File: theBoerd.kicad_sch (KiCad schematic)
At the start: 181 parts, among them SW1 SW_Push, U2 TRRS, U3 BlackPill_STLINK

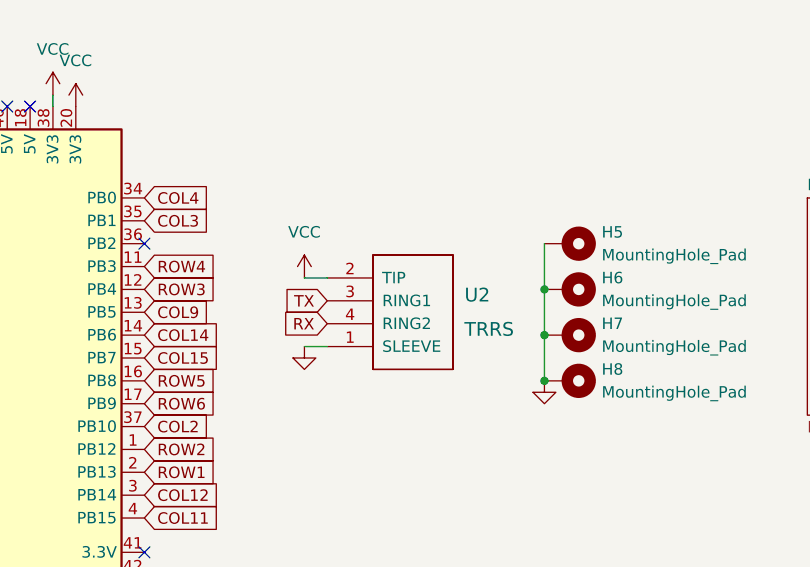
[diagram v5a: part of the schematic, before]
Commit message: Diode and Jack fixes, Silkscreen additons
Diode and TRRS Jack footprints replaced with available parts.
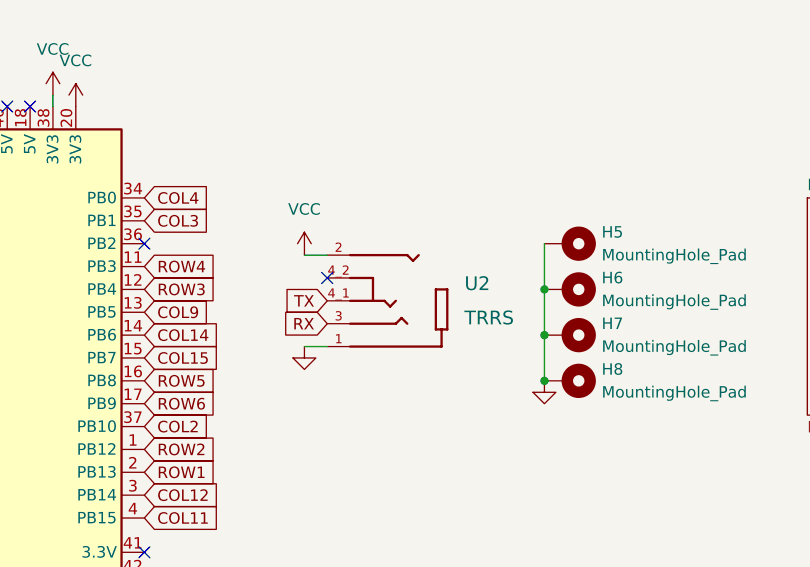
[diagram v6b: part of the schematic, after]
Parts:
- D1, D10, D11, D12, D13, D14, D15, D16, D17, D18, D19, D2, D20, D21, D22, D23, D24, D25, D26, D27, D28, D29, D3, D30, D31, D32, D33, D34, D35, D36, D37, D38, D39, D4, D40, D41, D42, D43, D44, D45, D46, D47, D48, D49, D5, D50, D51, D52, D53, D54, D55, D56, D57, D58, D59, D6, D60, D61, D62, D63, D64, D65, D66, D67, D68, D69, D7, D70, D71, D72, D73, D74, D75, D76, D77, D78, D79, D8, D80, D81, D82, D83, D84, D85, D86, D87, D9: footprint Diode_SMD:D_1210_3225Metric -> Diode_SMD:D_SOD-323_HandSoldering
- U2: footprint Keebio-Parts:TRRS-PJ-320A -> 54_00174:TENSILITY_54-00174; symbol keebio:TRRS -> 54-00174:54-00174; MANUFACTURER (none) -> TENSILITY; MAXIMUM_PACKAGE_HEIGHT (none) -> 6mm; PARTREV (none) -> A; SNAPEDA_PN (none) -> 54-00174; STANDARD (none) -> Manufacturer Recommendations
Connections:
- net RX: now also U2.3; no longer U2.4 (RING2)
- net TX: now also U2.4_1; no longer U2.3 (RING1)
- no-connect marks 15 -> 16

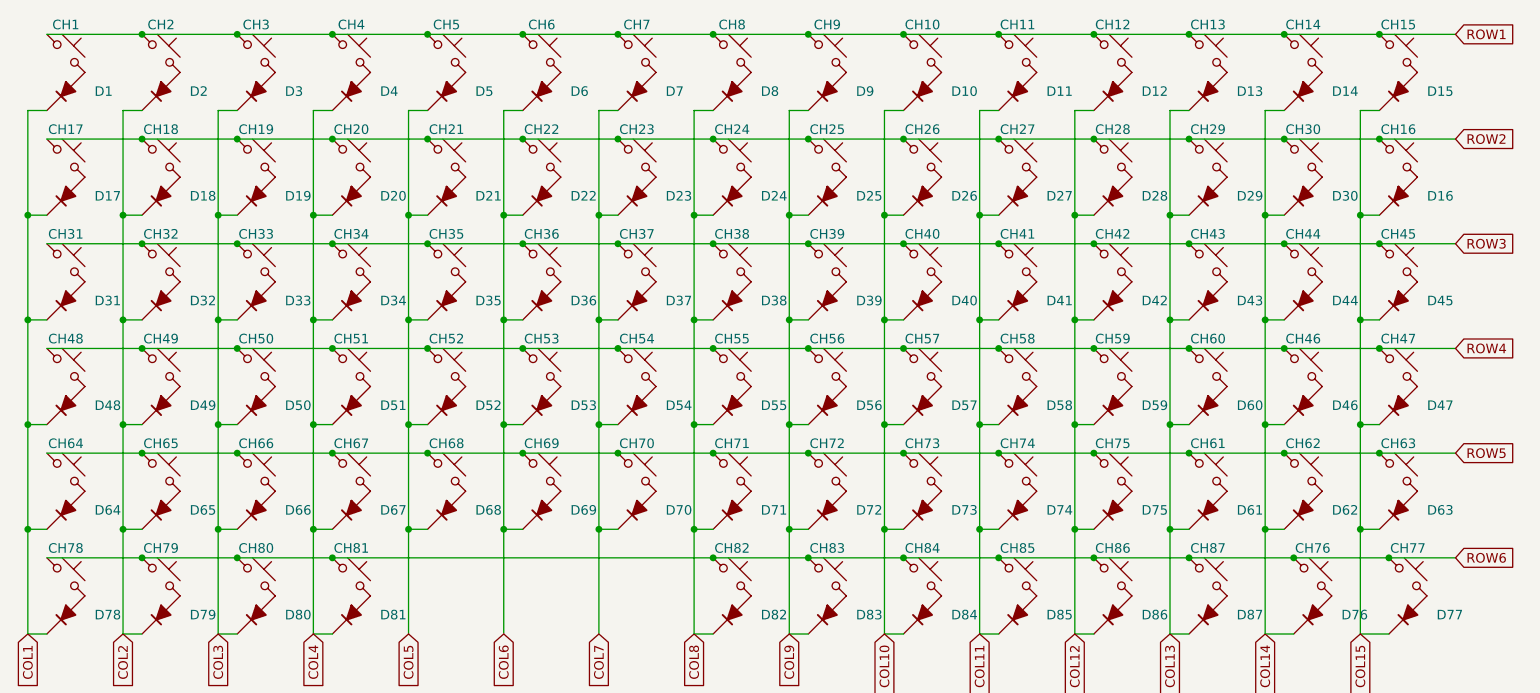
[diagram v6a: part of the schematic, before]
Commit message: Key Labeling
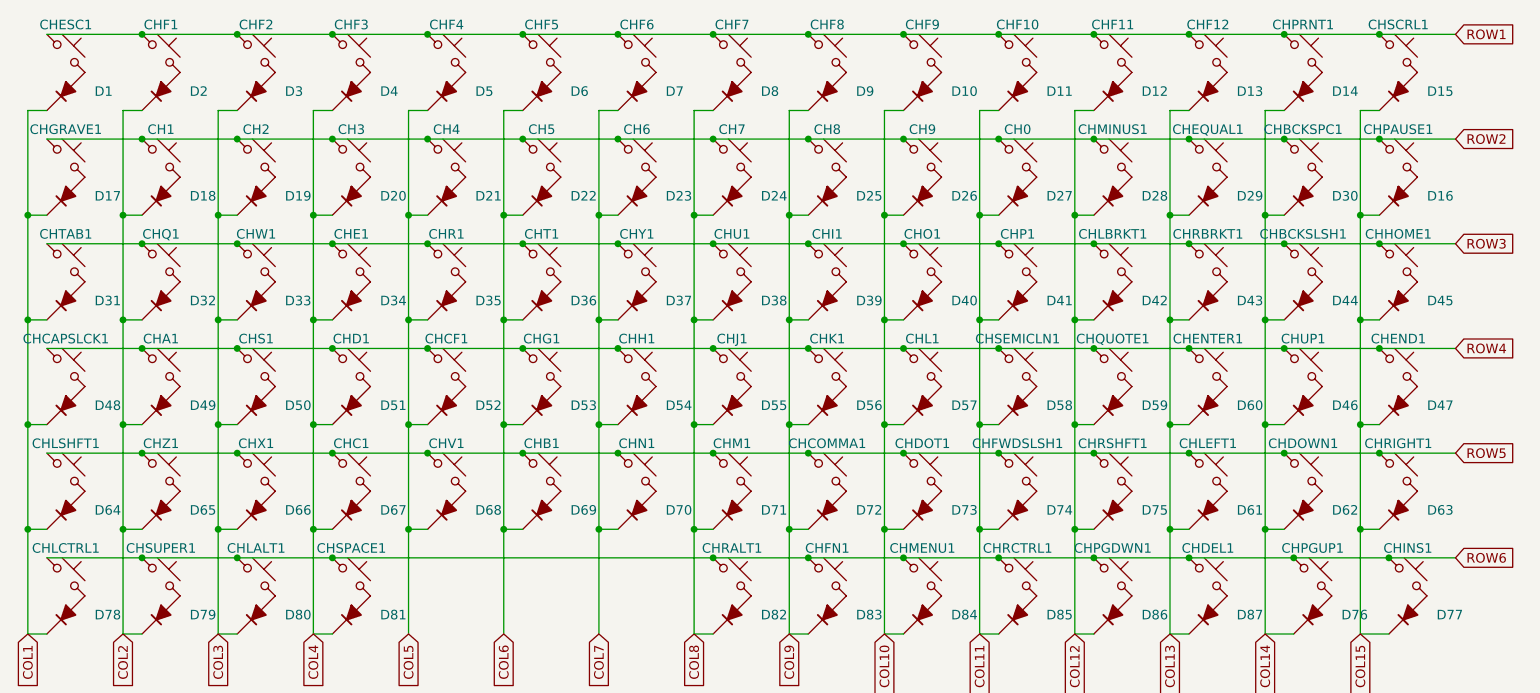
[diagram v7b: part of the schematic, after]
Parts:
- CHBCKSPC1: renamed from CH16; footprint MX_Hotswap:MX-Hotswap-1U -> MX_Hotswap:MX-Hotswap-2U
- CHEQUAL1: renamed from CH30; footprint MX_Hotswap:MX-Hotswap-2U -> MX_Hotswap:MX-Hotswap-1U
- renumbered CH28 to CH0, CH19 to CH1, CH20 to CH2, CH21 to CH3, CH22 to CH4, CH23 to CH5, CH24 to CH6, CH25 to CH7, CH26 to CH8, CH27 to CH9, CH49 to CHA1, CH69 to CHB1, CH44 to CHBCKSLSH1, CH67 to CHC1, CH48 to CHCAPSLCK1, CH52 to CHCF1, CH72 to CHCOMMA1, CH51 to CHD1, CH87 to CHDEL1, CH73 to CHDOT1, CH62 to CHDOWN1, CH34 to CHE1, CH47 to CHEND1, CH60 to CHENTER1, CH1 to CHESC1, CH2 to CHF1, CH11 to CHF10, CH12 to CHF11, CH13 to CHF12, CH3 to CHF2, CH4 to CHF3, CH5 to CHF4, CH6 to CHF5, CH7 to CHF6, CH8 to CHF7, CH9 to CHF8, CH10 to CHF9, CH83 to CHFN1, CH74 to CHFWDSLSH1, CH53 to CHG1, CH18 to CHGRAVE1, CH54 to CHH1, CH45 to CHHOME1, CH39 to CHI1, CH77 to CHINS1, CH55 to CHJ1, CH56 to CHK1, CH57 to CHL1, CH80 to CHLALT1, CH42 to CHLBRKT1, CH78 to CHLCTRL1, CH61 to CHLEFT1, CH64 to CHLSHFT1, CH71 to CHM1, CH84 to CHMENU1, CH29 to CHMINUS1, CH70 to CHN1, CH40 to CHO1, CH41 to CHP1, CH17 to CHPAUSE1, CH86 to CHPGDWN1, CH76 to CHPGUP1, CH14 to CHPRNT1, CH32 to CHQ1, CH59 to CHQUOTE1, CH35 to CHR1, CH82 to CHRALT1, CH43 to CHRBRKT1, CH85 to CHRCTRL1, CH63 to CHRIGHT1, CH75 to CHRSHFT1, CH50 to CHS1, CH15 to CHSCRL1, CH58 to CHSEMICLN1, CH81 to CHSPACE1, CH79 to CHSUPER1, CH36 to CHT1, CH31 to CHTAB1, CH38 to CHU1, CH46 to CHUP1, CH68 to CHV1, CH33 to CHW1, CH66 to CHX1, CH37 to CHY1, CH65 to CHZ1
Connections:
- net at D25.2 (A): now also CH8.2; no longer CH7.2
- net at D27.2 (A): now also CH0.2; no longer CH9.2
- net at CH5.2: now also D22.2 (A); no longer D23.2 (A)
- net at CH6.2: now also D23.2 (A); no longer D24.2 (A)
- net at D17.2 (A): now also CHGRAVE1.2; no longer CHPAUSE1.2
- net at D19.2 (A): now also CH2.2; no longer CH1.2
- net at CH3.2: now also D20.2 (A); no longer D21.2 (A)
- net at D30.2 (A): now also CHBCKSPC1.2; no longer CHEQUAL1.2
- net at D16.2 (A): now also CHPAUSE1.2; no longer CHBCKSPC1.2
- net at D26.2 (A): now also CH9.2; no longer CH8.2
- net at D18.2 (A): now also CH1.2; no longer CHGRAVE1.2
- net at CHMINUS1.2: now also D28.2 (A); no longer D29.2 (A)
- net at CH4.2: now also D21.2 (A); no longer D22.2 (A)
- new net: CH7.2, D24.2 (A)
- new net: CHEQUAL1.2, D29.2 (A)
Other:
- moved on the sheet: CH0, CH1, CH2, CH3, CH4, CH5, CH6, CH7, CH8, CH9, CHBCKSPC1, CHEQUAL1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

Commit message: PDF Exports
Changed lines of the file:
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@@
 				)
 				(justify left)
-				(hide yes)
 			)
 		)
@@
 				)
 				(justify left)
-				(hide yes)
 			)
 		)
@@
 				)
 				(justify right)
-				(hide yes)
 			)
 		)
@@
 				)
 				(justify left)
-				(hide yes)
 			)
 		)
@@
 				)
 				(justify left)
-				(hide yes)
 			)
 		)
@@
 				)
 				(justify right)
-				(hide yes)
 			)
 		)
@@
 				)
 				(justify right)
-				(hide yes)
 			)
 		)
@@
 				)
 				(justify right)
-				(hide yes)
 			)
 		)
@@
 				)
 				(justify right)
-				(hide yes)
 			)
 		)
@@
 				)
 				(justify right)
-				(hide yes)
 			)
 		)
@@
 				)
 				(justify right)
-				(hide yes)
 			)
 		)
@@
 				)
 				(justify left)
-				(hide yes)
 			)
 		)
@@
 				)
 				(justify right)
-				(hide yes)
 			)
 		)
@@
 				)
 				(justify right)
-				(hide yes)
 			)
 		)
@@
 				)
 				(justify right)
-				(hide yes)
 			)
 		)
@@
 				)
 				(justify left)
-				(hide yes)
 			)
 		)
@@
 				)
 				(justify left)
-				(hide yes)
 			)
 		)
@@
 				)
 				(justify right)
-				(hide yes)
 			)
 		)
@@
 				)
 				(justify right)
-				(hide yes)
 			)
 		)
@@
 				)
 				(justify right)
-				(hide yes)
 			)
 		)
@@
 				)
 				(justify right)
-				(hide yes)
 			)
 		)
@@
 				)
 				(justify left)
-				(hide yes)
 			)
 		)
@@
 				)
 				(justify right)
-				(hide yes)
 			)
 		)
@@
 				)
 				(justify right)
-				(hide yes)
 			)
 		)
@@
 				)
 				(justify left)
-				(hide yes)
 			)
 		)
@@
 				)
 				(justify left)
-				(hide yes)
 			)
 		)
@@
 				)
 				(justify left)
-				(hide yes)
 			)
 		)
@@
 				)
 				(justify right)
-				(hide yes)
 			)
 		)
@@
 				)
 				(justify right)
-				(hide yes)
 			)
 		)
@@
 				)
 				(justify left)
-				(hide yes)
 			)
 		)
@@
 				)
 				(justify left)
-				(hide yes)
 			)
 		)
@@
 				)
 				(justify right)
-				(hide yes)
 			)
 		)
@@
 				)
 				(justify right)
-				(hide yes)
 			)
 		)
@@
 				)
 				(justify left)
-				(hide yes)
 			)
 		)
@@
 				)
 				(justify left)
-				(hide yes)
 			)
 		)
@@
 				)
 				(justify right)
-				(hide yes)
 			)
 		)
@@
 				)
 				(justify right)
-				(hide yes)
 			)
 		)
@@
 				)
 				(justify right)
-				(hide yes)
 			)
 		)
@@
 				)
 				(justify left)
-				(hide yes)
 			)
 		)
@@
 				)
 				(justify left)
-				(hide yes)
 			)
 		)
@@
 				)
 				(justify right)
-				(hide yes)
 			)
 		)
@@
 				)
 				(justify left)
-				(hide yes)
 			)
 		)
@@
 				)
 				(justify right)
-				(hide yes)
 			)
 		)
@@
 				)
 				(justify right)
-				(hide yes)
 			)
 		)
@@
 				)
 				(justify left)
-				(hide yes)
 			)
 		)
@@
 				)
 				(justify left)
-				(hide yes)
 			)
 		)
@@
 	)
 	(sheet
-		(at 133.35 130.81)
-		(size 26.67 24.13)
+		(at 82.55 162.56)
+		(size 12.7 15.24)
 		(exclude_from_sim no)
 		(in_bom yes)
@@
 		)
 		(property "Sheetname" "NumPad"
-			(at 133.35 130.0984 0)
+			(at 82.55 161.8484 0)
+			(show_name yes)
 			(effects
 				(font
@@
 		)
 		(property "Sheetfile" "numpad.kicad_sch"
-			(at 133.35 155.5246 0)
+			(at 82.55 178.3846 0)
 			(effects
 				(font
